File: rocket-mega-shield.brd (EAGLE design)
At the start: 114.3 x 60 mm, 64 parts, among them J1 ExtBatt, J2 Mega R3, J3 XBEE, J4 MICROSD, J5 U.FL, J6 1X6TERMINALBLOCK, Q1 BSS138, Q2 BSS138, Q3 BSS138, Q4 SI7112DN, Q5 SI7112DN, Q6 SI7112DN, Q7 SI7112DN, U1 NCP1117DT33G, U2 M74HC4050M, U3 FGPMMOPA6H, U4 BMP180, U5 LSM303DLHCTR, U6 L3GD20TR, U7 ADXL377

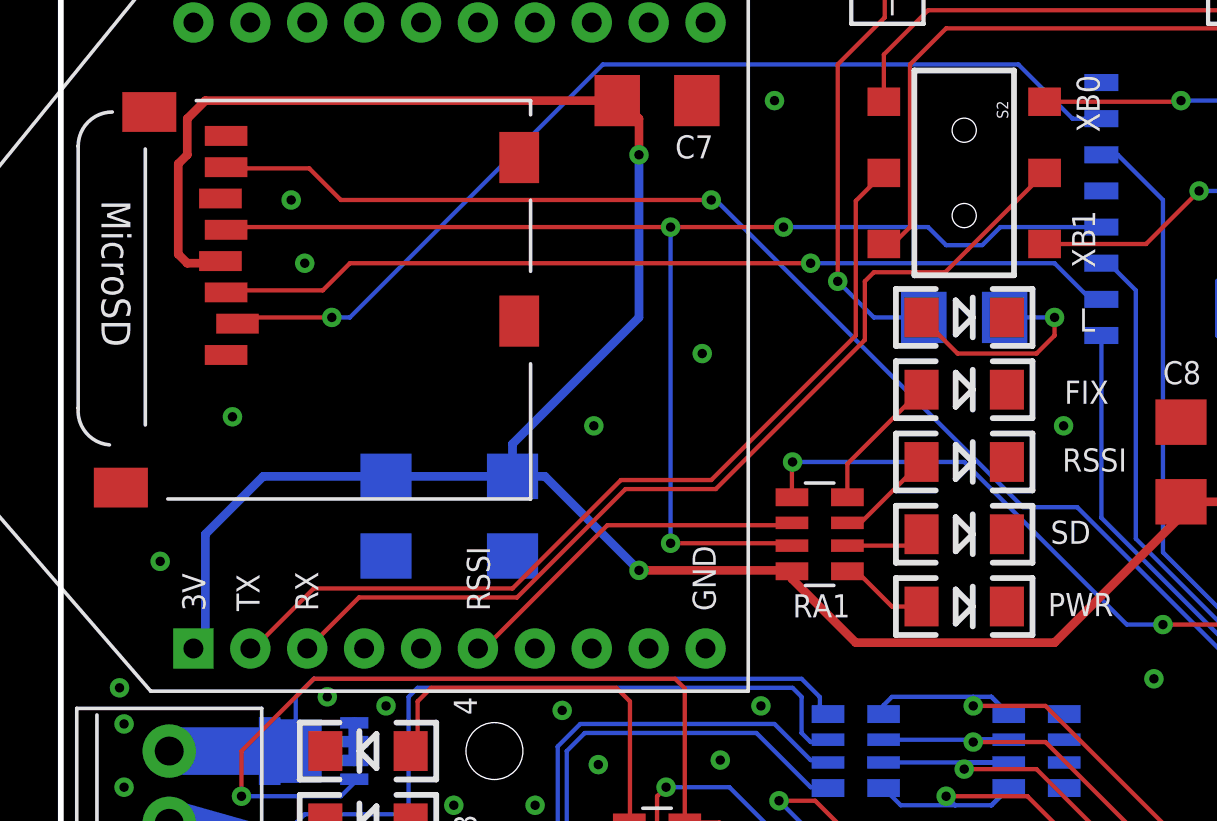
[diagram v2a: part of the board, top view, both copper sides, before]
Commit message: slight update to labelling and routing around xbee
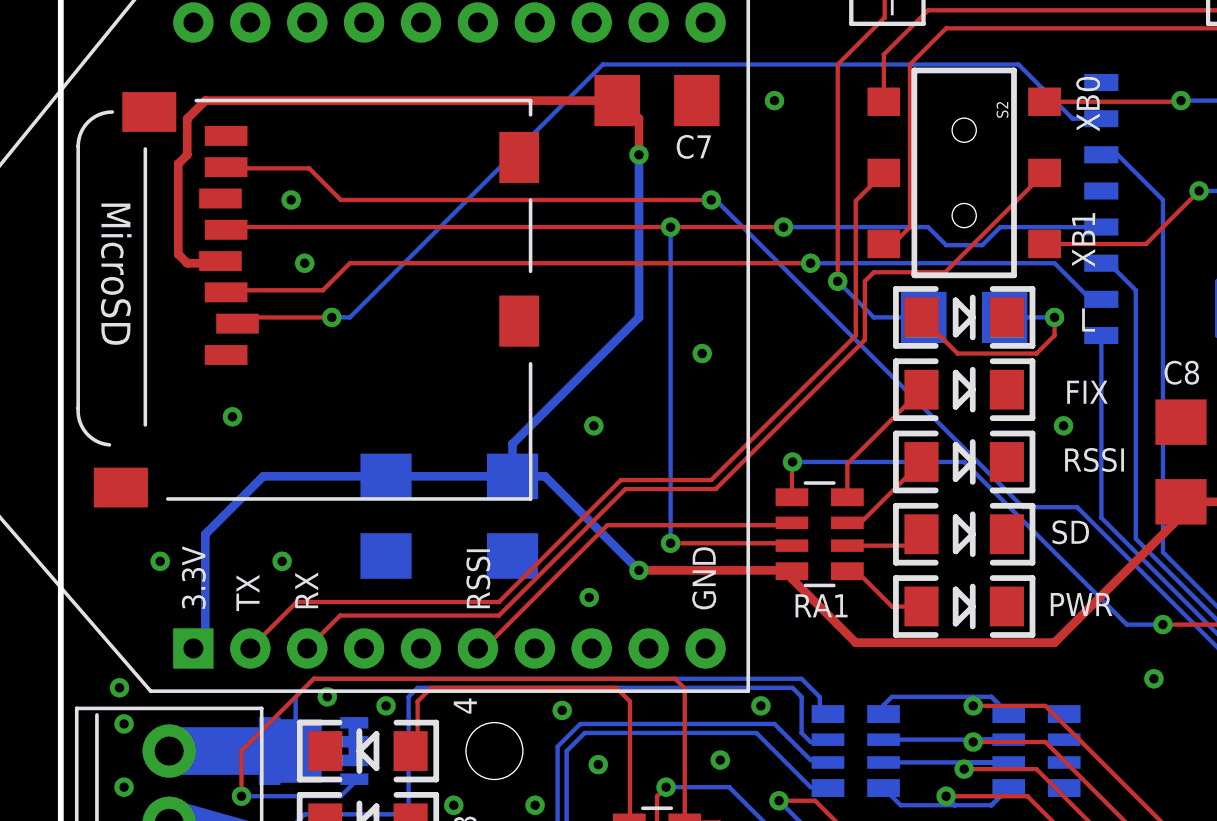
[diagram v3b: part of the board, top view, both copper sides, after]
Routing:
- net GND: vias 75 -> 77
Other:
- board text added: "3.3V"
- board text removed: "3V"
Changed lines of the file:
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@@
 <text x="15.875" y="30.32125" size="0.8128" layer="21" ratio="12" rot="R90">TX</text>
 <text x="17.93875" y="30.32125" size="0.8128" layer="21" ratio="12" rot="R90">RX</text>
-<text x="13.97" y="30.32125" size="0.8128" layer="21" ratio="12" rot="R90">3V</text>
+<text x="13.97" y="30.32125" size="0.8128" layer="21" ratio="12" rot="R90">3.3V</text>
 <text x="23.97125" y="30.32125" size="0.8128" layer="21" ratio="12" rot="R90">RSSI</text>
 <text x="31.90875" y="30.32125" size="0.8128" layer="21" ratio="12" rot="R90">GND</text>
@@
 <via x="89.8525" y="40.005" extent="1-16" drill="0.3302"/>
 <via x="80.9625" y="34.29" extent="1-16" drill="0.3302"/>
+<via x="16.66875" y="32.0675" extent="1-16" drill="0.3302"/>
+<via x="27.46375" y="30.7975" extent="1-16" drill="0.3302"/>
 </signal>
 <signal name="VCC3" class="1">
@@
 <contactref element="S2" pad="5"/>
 <contactref element="J3" pad="2"/>
-<wire x1="15.55" y1="29.005" x2="15.67" y2="29.005" width="0.1524" layer="1"/>
-<wire x1="15.67" y1="29.005" x2="17.78" y2="31.115" width="0.1524" layer="1"/>
-<wire x1="17.78" y1="31.115" x2="24.765" y2="31.115" width="0.1524" layer="1"/>
-<wire x1="24.765" y1="31.115" x2="28.575" y2="34.925" width="0.1524" layer="1"/>
+<wire x1="24.28875" y1="30.63875" x2="28.575" y2="34.925" width="0.1524" layer="1"/>
 <wire x1="28.575" y1="34.925" x2="31.75" y2="34.925" width="0.1524" layer="1"/>
 <wire x1="31.75" y1="34.925" x2="36.83" y2="40.005" width="0.1524" layer="1"/>
 <wire x1="36.83" y1="40.005" x2="36.83" y2="44.735" width="0.1524" layer="1"/>
 <wire x1="36.83" y1="44.735" x2="37.815" y2="45.72" width="0.1524" layer="1"/>
+<wire x1="24.28875" y1="30.63875" x2="17.18375" y2="30.63875" width="0.1524" layer="1"/>
+<wire x1="17.18375" y1="30.63875" x2="15.55" y2="29.005" width="0.1524" layer="1"/>
 </signal>
 <signal name="N$22">
 <contactref element="J3" pad="3"/>
 <contactref element="S2" pad="2"/>
-<wire x1="17.55" y1="29.005" x2="17.575" y2="29.005" width="0.1524" layer="1"/>
-<wire x1="17.575" y1="29.005" x2="19.3675" y2="30.7975" width="0.1524" layer="1"/>
-<wire x1="19.3675" y1="30.7975" x2="24.92375" y2="30.7975" width="0.1524" layer="1"/>
-<wire x1="24.92375" y1="30.7975" x2="28.73375" y2="34.6075" width="0.1524" layer="1"/>
+<wire x1="24.28875" y1="30.1625" x2="28.73375" y2="34.6075" width="0.1524" layer="1"/>
 <wire x1="28.73375" y1="34.6075" x2="31.90875" y2="34.6075" width="0.1524" layer="1"/>
-<wire x1="40.76625" y1="43.02125" x2="42.37" y2="44.625" width="0.1524" layer="1"/>
-<wire x1="42.37" y1="44.625" x2="43.465" y2="45.72" width="0.1524" layer="1"/>
+<wire x1="39.9725" y1="42.2275" x2="43.465" y2="45.72" width="0.1524" layer="1"/>
 <wire x1="31.90875" y1="34.6075" x2="37.1475" y2="39.84625" width="0.1524" layer="1"/>
 <wire x1="37.1475" y1="39.84625" x2="37.1475" y2="41.91" width="0.1524" layer="1"/>
 <wire x1="37.1475" y1="41.91" x2="37.465" y2="42.2275" width="0.1524" layer="1"/>
 <wire x1="37.465" y1="42.2275" x2="39.9725" y2="42.2275" width="0.1524" layer="1"/>
-<wire x1="39.9725" y1="42.2275" x2="40.76625" y2="43.02125" width="0.1524" layer="1"/>
+<wire x1="24.28875" y1="30.1625" x2="18.7075" y2="30.1625" width="0.1524" layer="1"/>
+<wire x1="18.7075" y1="30.1625" x2="17.55" y2="29.005" width="0.1524" layer="1"/>
 </signal>
 <signal name="SDCS">

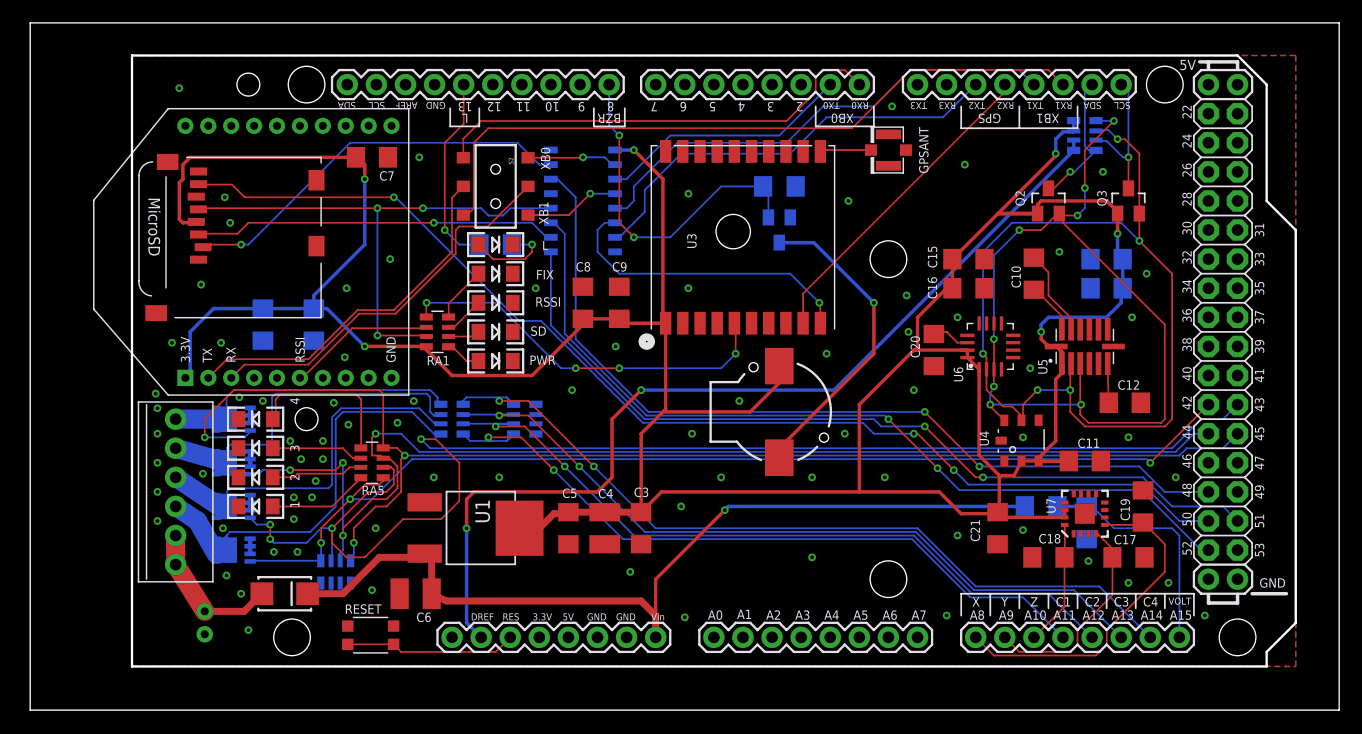
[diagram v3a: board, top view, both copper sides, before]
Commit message: changed out mosfet on speaker for higher amperage, more cleanup
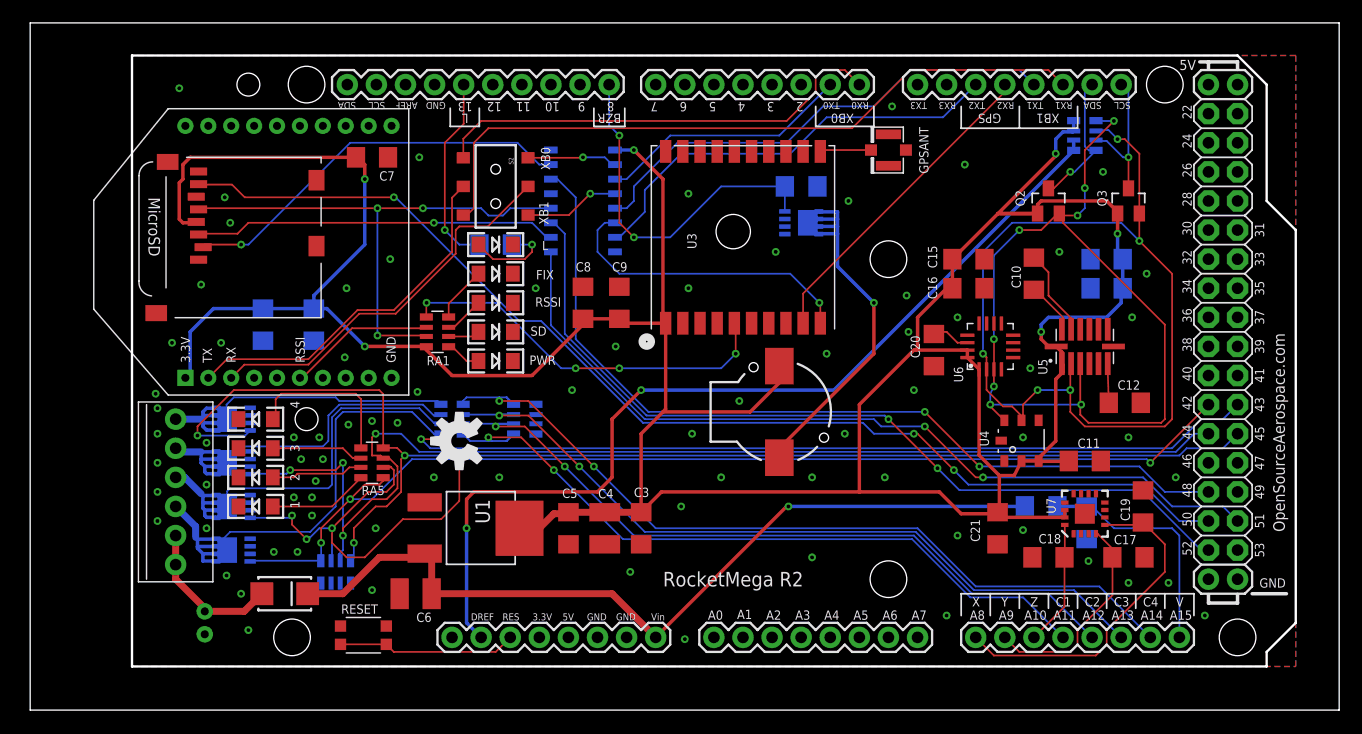
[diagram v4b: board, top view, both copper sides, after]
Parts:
- added LOGO1: OSHW-LOGOM, SparkFun-Aesthetics:OSHW-LOGO-M
- Q1: value BSS138 -> SI7112DN; device kurt:SOT23 -> SparkFun-DiscreteSemi:POWERPAK1212-8
- R1, RA3: value 110k -> 100k
- moved Q1 2.01 mm to (67.3, 42.5)
- moved R4 1.91 mm to (67.3, 45.7)
- moved S1 0.64 mm to (31.6, 5.24)
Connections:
- net GND: now also Q1.S1, Q1.S2, Q1.S3; no longer Q1.2
- net MEGA8: now also Q1.G; no longer Q1.1
- net N$13: now also Q1.D1, Q1.D2, Q1.D3, Q1.D4, Q1.DPAD; no longer Q1.3
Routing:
- net N$13: track 28.2 -> 34.7 mm
- net GND: track 5.28 -> 0.00 mm
- net VIN: track 77.5 -> 73.5 mm
- net N$3: track 38.4 -> 41.9 mm
- net N$4: track 34.7 -> 37.4 mm
- net MEGA8: track 30.3 -> 31.4 mm
- net N$24: track 31.2 -> 30.1 mm
- net PYRO4: track 115.1 -> 115.9 mm
- net N$25: track 33.5 -> 32.8 mm
- net RESET: track 15.0 -> 15.6 mm
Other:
- board text added: "OpenSourceAerospace.com"
- board text added: "RocketMega R2"
- board text added: "V"
- board text removed: "VOLT"

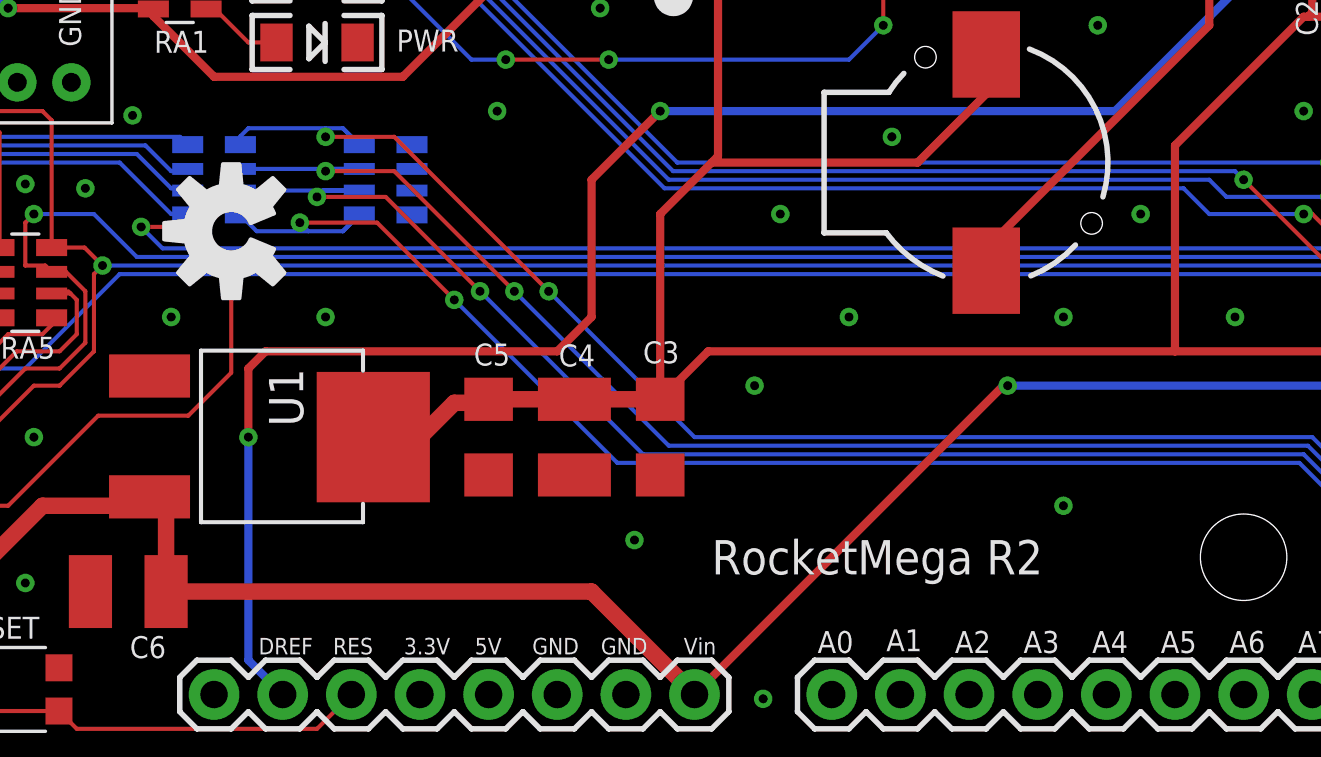
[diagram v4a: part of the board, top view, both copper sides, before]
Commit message: changed mosfet for speaker, added osaerospace logo
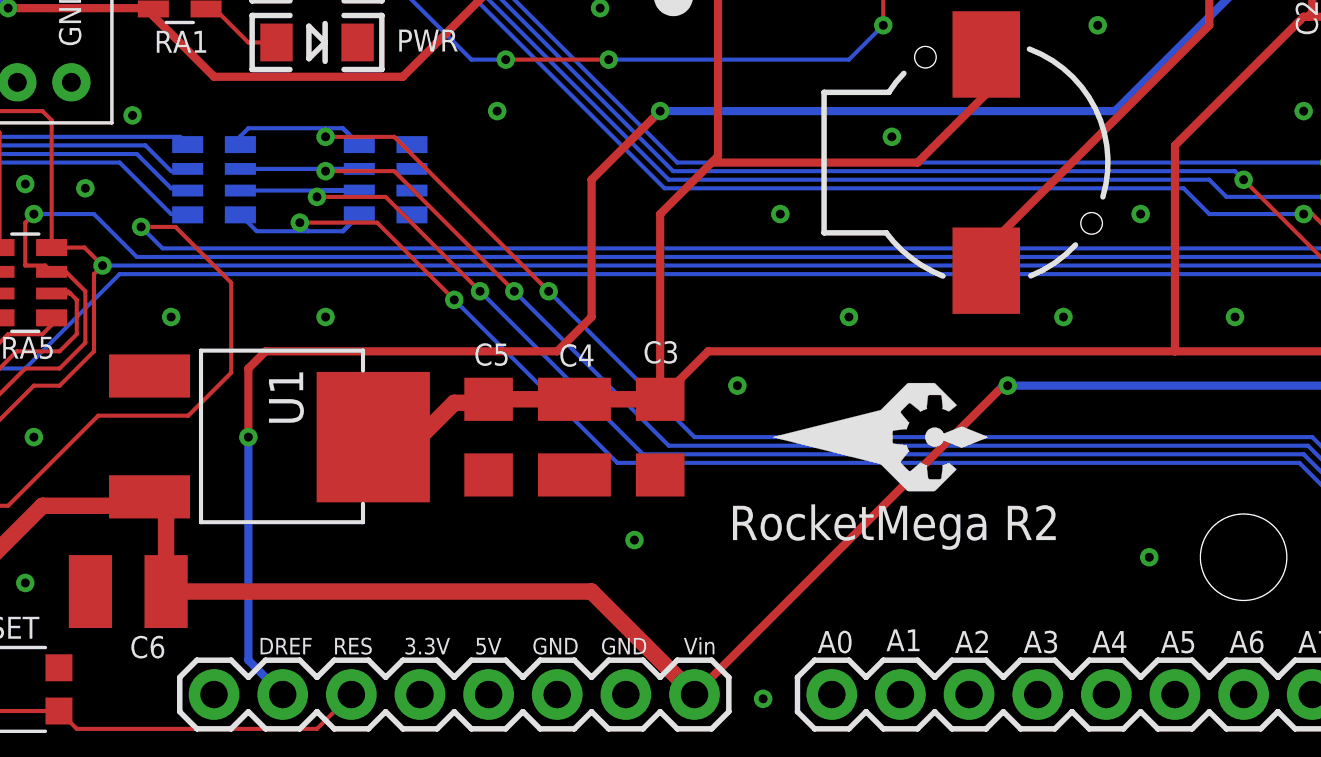
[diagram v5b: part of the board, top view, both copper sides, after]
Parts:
- added U$1: OSAEROSPACEVECTOR, zortness:OSAEROSPACE_V
- moved LOGO1 62.5 mm to (96.2, 44.9), flipped to the bottom, turned to 270 degrees
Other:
- board text added: "Open Source Hardware"
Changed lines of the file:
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@@
 <wire x1="101.6" y1="10.16" x2="101.6" y2="8.255" width="0.1524" layer="21"/>
 <text x="109.5375" y="15.5575" size="1.016" layer="21" ratio="12" rot="R90">OpenSourceAerospace.com</text>
-<text x="55.245" y="10.795" size="1.27" layer="21" ratio="12">RocketMega R2</text>
+<text x="55.88" y="12.065" size="1.27" layer="21" ratio="12">RocketMega R2</text>
+<text x="99.695" y="49.53" size="1.27" layer="22" ratio="12" rot="SMR270">Open Source Hardware</text>
 </plain>
 <attributes>
@@
 <attribute name="NAME" x="39.71925" y="42.672" size="0.8128" layer="26" rot="MR180"/>
 </element>
-<element name="LOGO1" library="SparkFun-Aesthetics" package="OSHW-LOGO-M" value="OSHW-LOGOM" x="37.465" y="23.495" rot="R90"/>
+<element name="LOGO1" library="SparkFun-Aesthetics" package="OSHW-LOGO-M" value="OSHW-LOGOM" x="96.2025" y="44.92625" rot="MR270"/>
 <element name="Q1" library="SparkFun-DiscreteSemi" package="POWERPAK1212-8" value="SI7112DN" x="67.31" y="42.545" smashed="yes" rot="MR180">
 <attribute name="PROD_ID" value="TRANS-11055" x="67.31" y="42.545" size="1.016" layer="28" ratio="12" rot="MR180" display="off"/>
 <attribute name="NAME" x="66.32575" y="40.54475" size="0.8128" layer="26" rot="MR180"/>
 </element>
+<element name="U$1" library="zortness" package="OSAEROSPACE_V" value="OSAEROSPACEVECTOR" x="63.5" y="15.875" rot="R90"/>
 </elements>
 <signals>
@@
 <via x="95.885" y="23.8125" extent="1-16" drill="0.3302"/>
 <via x="80.01" y="8.255" extent="1-16" drill="0.3302"/>
-<via x="68.2625" y="13.335" extent="1-16" drill="0.3302"/>
-<via x="56.8325" y="17.78" extent="1-16" drill="0.3302"/>
+<via x="71.4375" y="11.43" extent="1-16" drill="0.3302"/>
+<via x="56.1975" y="17.78" extent="1-16" drill="0.3302"/>
 <via x="27.78125" y="24.92375" extent="1-16" drill="0.3302"/>
 <via x="24.92375" y="20.0025" extent="1-16" drill="0.3302"/>
